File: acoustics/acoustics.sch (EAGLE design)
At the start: 40 parts, among them IC1 ADS8322, IC2 ADS8322, IC3 ADS8322, IC4 ADS8322

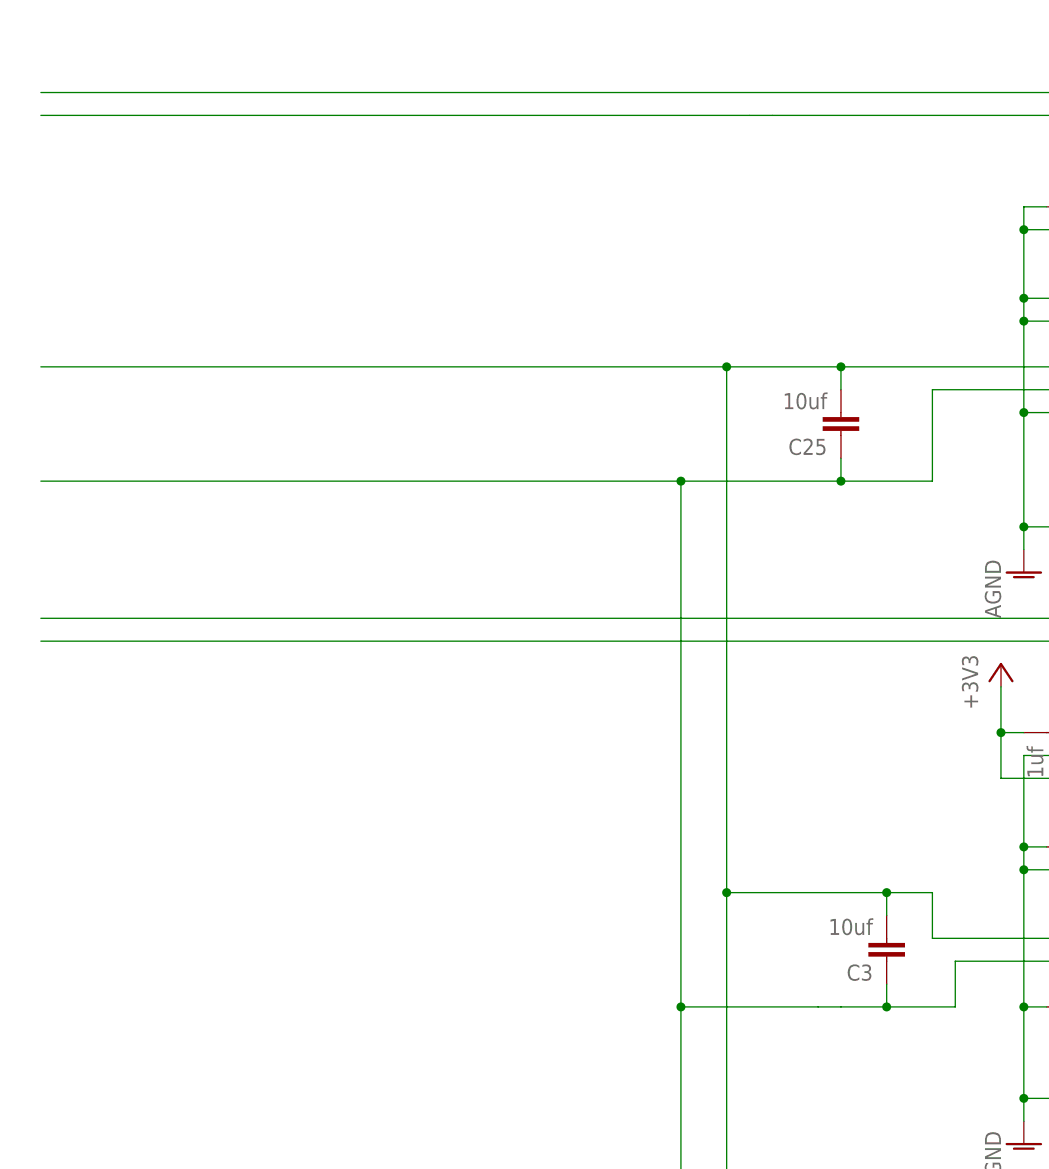
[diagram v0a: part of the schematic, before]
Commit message: Added acoustics reference generator
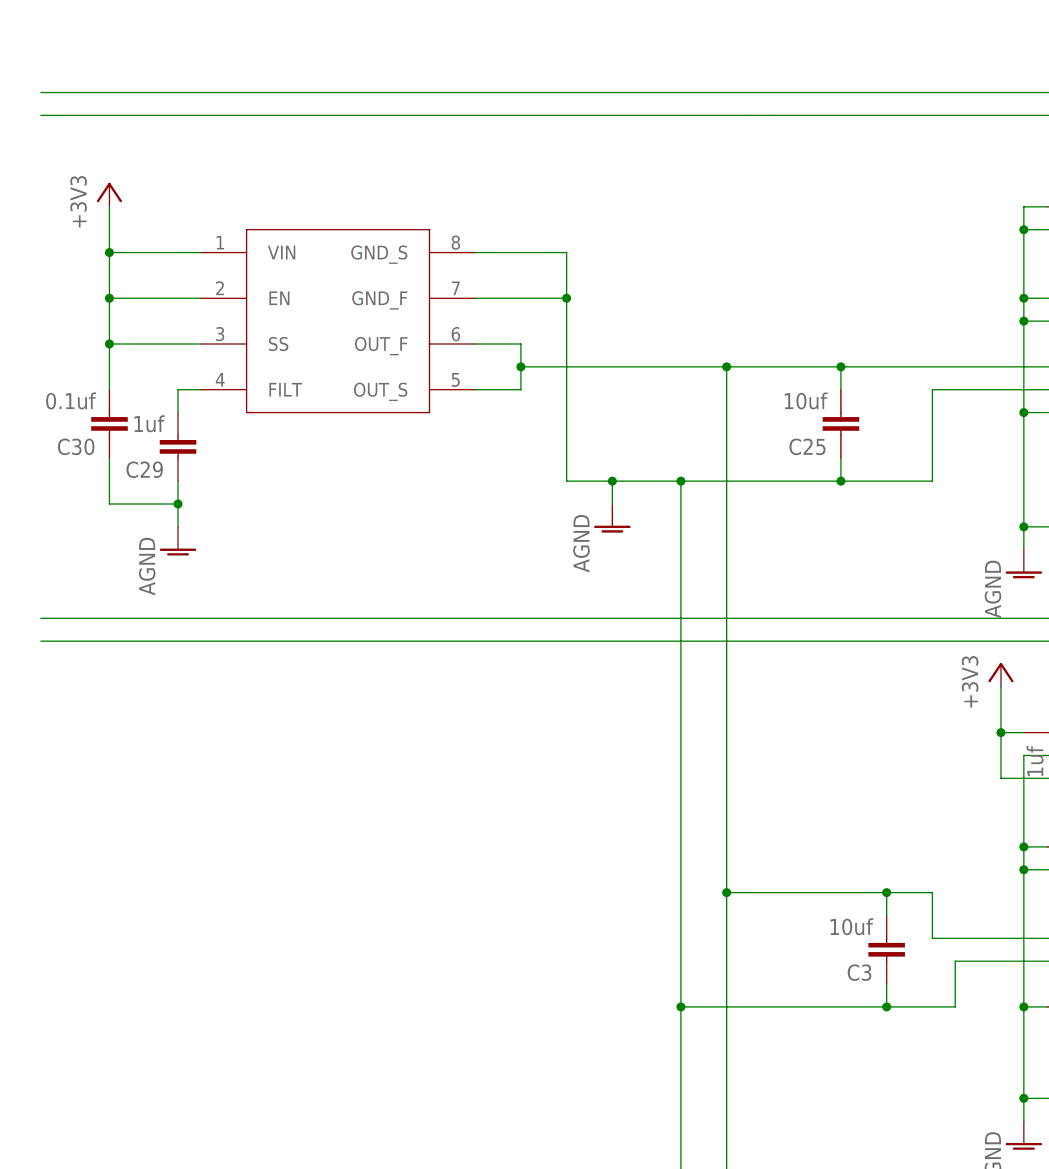
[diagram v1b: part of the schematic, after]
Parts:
- added C29: 1uf, rcl:C-EUC0805K
- added C30: 0.1uf, rcl:C-EUC0805K
- added U$1: REF6025, REF6025:REF6025
- C1, C10, C11, C12, C13, C14, C15, C16, C17, C18, C19, C2, C20, C21, C22, C23, C24, C25, C26, C27, C28, C3, C4, C5, C6, C7, C8, C9: device resistor:C-EU050-025X075 -> rcl:C-EUC0805K
- R1, R2, R3, R4, R5, R6, R7, R8: device resistor:R-US_0309/12 -> rcl:R-US_M0805
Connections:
- removed net N$5: C18.1, C25.1, C3.1, C8.1, IC1.REFN, IC2.REFN, IC3.REFN, IC4.REFN
- new net N$2: C29.2, U$1.FILT
- net +3V3: now also C30.2, U$1.EN, U$1.SS, U$1.VIN
- net AGND: now also C18.1, C25.1, C29.1, C3.1, C30.1, C8.1, IC1.REFN, IC2.REFN, IC3.REFN, IC4.REFN, U$1.GND_F, U$1.GND_S
- net N$19: now also U$1.OUT_F, U$1.OUT_S

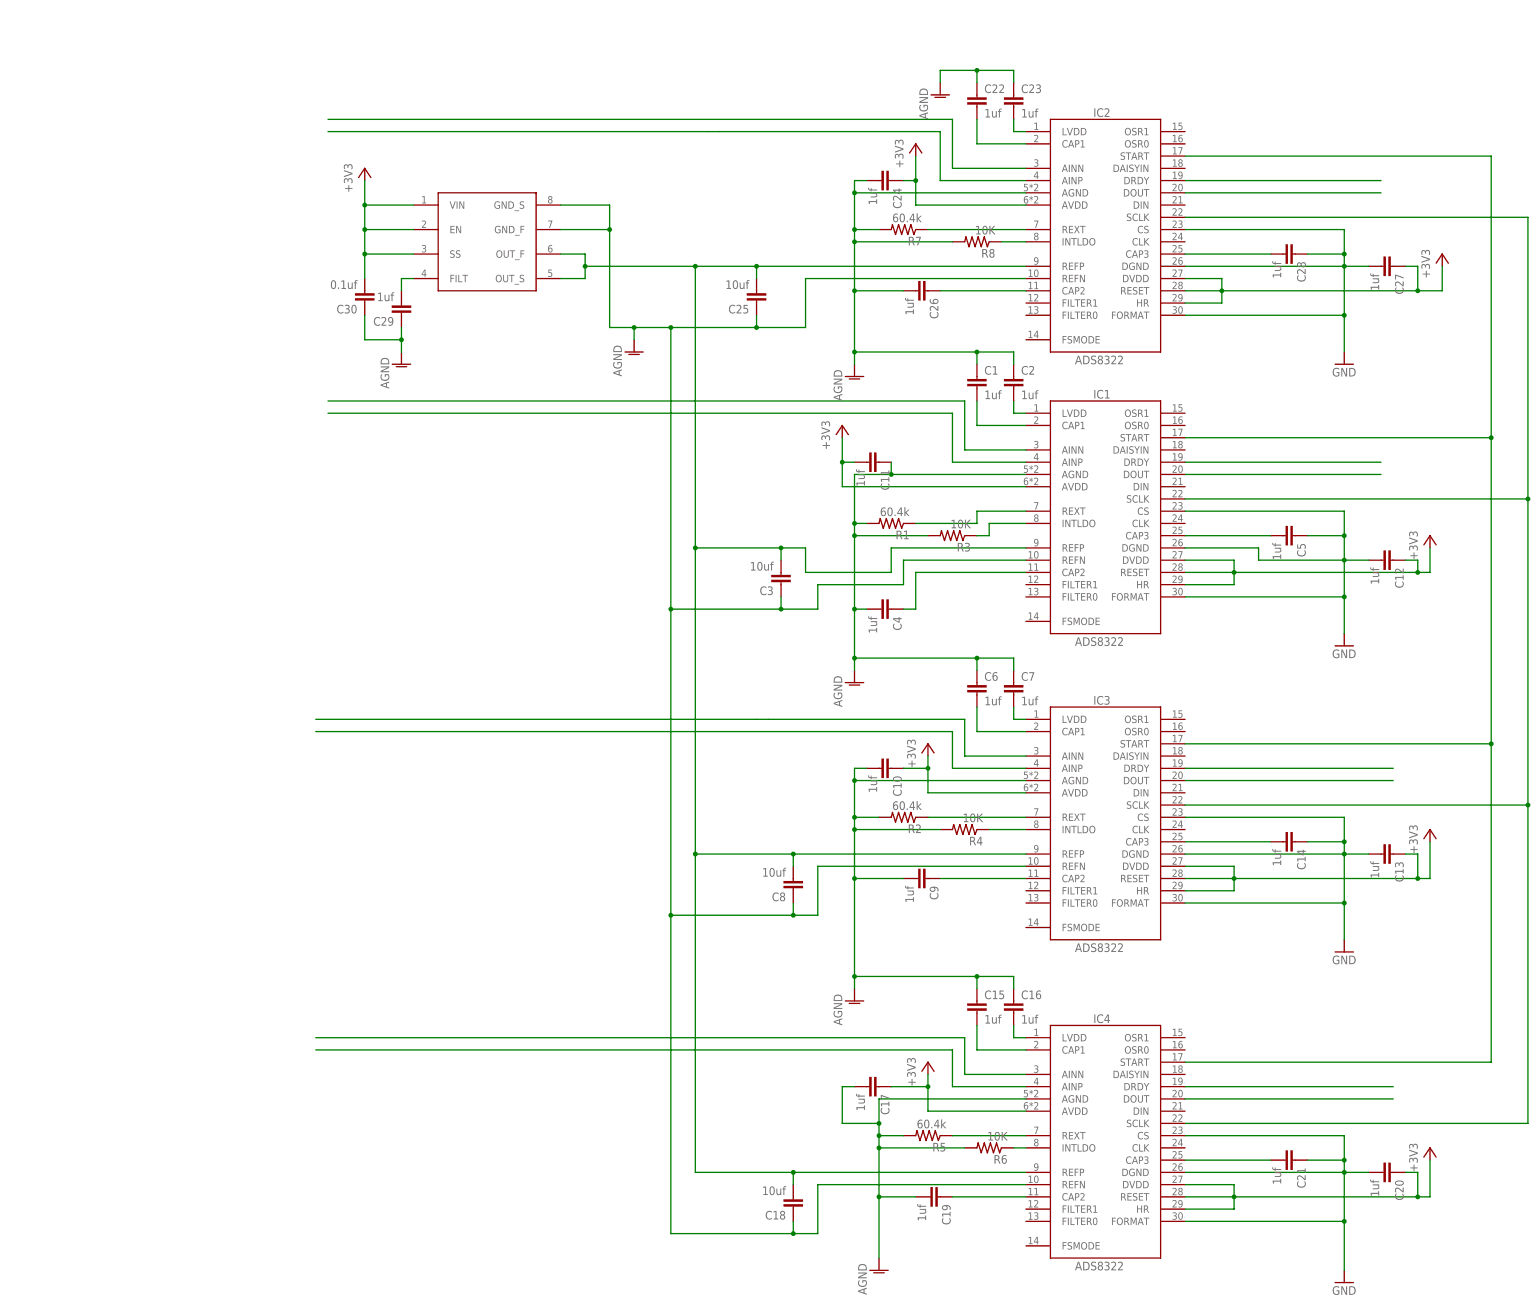
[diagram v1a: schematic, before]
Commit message: Added THS VSSOP-8 package, added reference data sheets
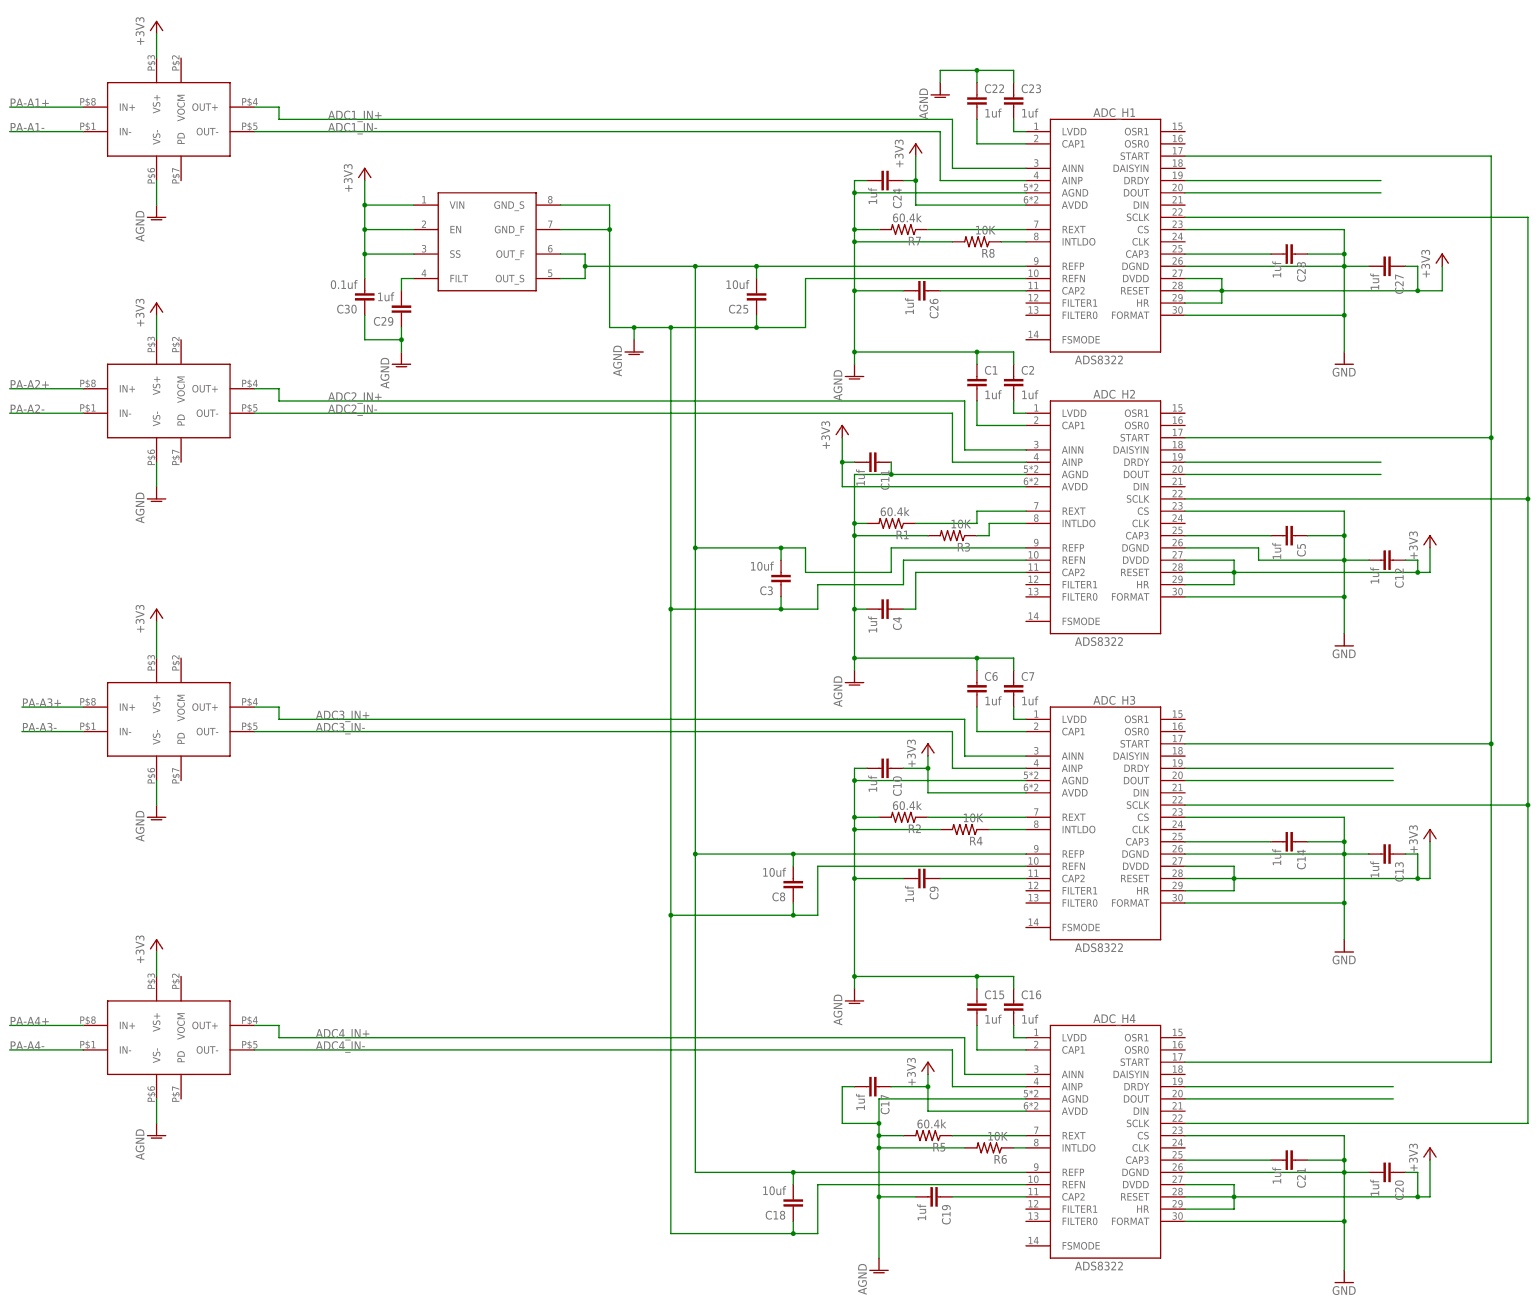
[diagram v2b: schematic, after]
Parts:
- added U$2, U$3, U$4, U$5: THS4551, THS4551:THS4551
- renumbered IC1 to ADC_H2, IC2 to ADC_H1, IC3 to ADC_H3, IC4 to ADC_H4
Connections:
- net N$10 renamed DOUT_H2
- net N$25 renamed DRDY_H3
- net N$26 renamed DOUT_H3
- net N$27 renamed SCLK
- net N$36 renamed DRDY_H4
- net N$37 renamed DOUT_H4
- net N$51 renamed DRDY_H1
- net N$52 renamed DOUT_H1
- net N$7 renamed DRDY_H2
- removed net N$14: ADC_H2.AINN
- removed net N$15: ADC_H2.AINP
- removed net N$16: ADC_H3.AINN
- removed net N$17: ADC_H3.AINP
- removed net N$28: ADC_H4.AINN
- removed net N$29: ADC_H4.AINP
- removed net N$41: ADC_H1.AINN
- removed net N$42: ADC_H1.AINP
- new net ADC1_IN+: ADC_H1.AINN, U$2.OUT+
- new net ADC1_IN-: ADC_H1.AINP, U$2.OUT-
- new net ADC2_IN+: ADC_H2.AINN, U$3.OUT+
- new net ADC2_IN-: ADC_H2.AINP, U$3.OUT-
- new net ADC3_IN+: ADC_H3.AINN, U$4.OUT+
- new net ADC3_IN-: ADC_H3.AINP, U$4.OUT-
- new net ADC4_IN+: ADC_H4.AINN, U$5.OUT+
- new net ADC4_IN-: ADC_H4.AINP, U$5.OUT-
- new net PA-A1+: U$2.IN+
- new net PA-A1-: U$2.IN-
- new net PA-A2+: U$3.IN+
- new net PA-A2-: U$3.IN-
- new net PA-A3+: U$4.IN+
- new net PA-A3-: U$4.IN-
- new net PA-A4+: U$5.IN+
- new net PA-A4-: U$5.IN-
- net +3V3: now also U$2.VS+, U$3.VS+, U$4.VS+, U$5.VS+
- net AGND: now also U$2.VS-, U$3.VS-, U$4.VS-, U$5.VS-
